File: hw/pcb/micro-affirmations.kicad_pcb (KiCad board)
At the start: 2 copper layers, 100 x 100 mm, 47 parts, among them J1 USB-C_2171750001, Q1 SSM3K37FSLF, Q10 SSM3K37FSLF, Q2 SSM3K37FSLF, Q3 SSM3K37FSLF, Q4 SSM3K37FSLF, Q5 SSM3K37FSLF, Q6 SSM3K37FSLF, Q7 SSM3K37FSLF, Q8 SSM3K37FSLF, Q9 SSM3K37FSLF, SW1 SW_Push, U1 STM32C031C6Tx

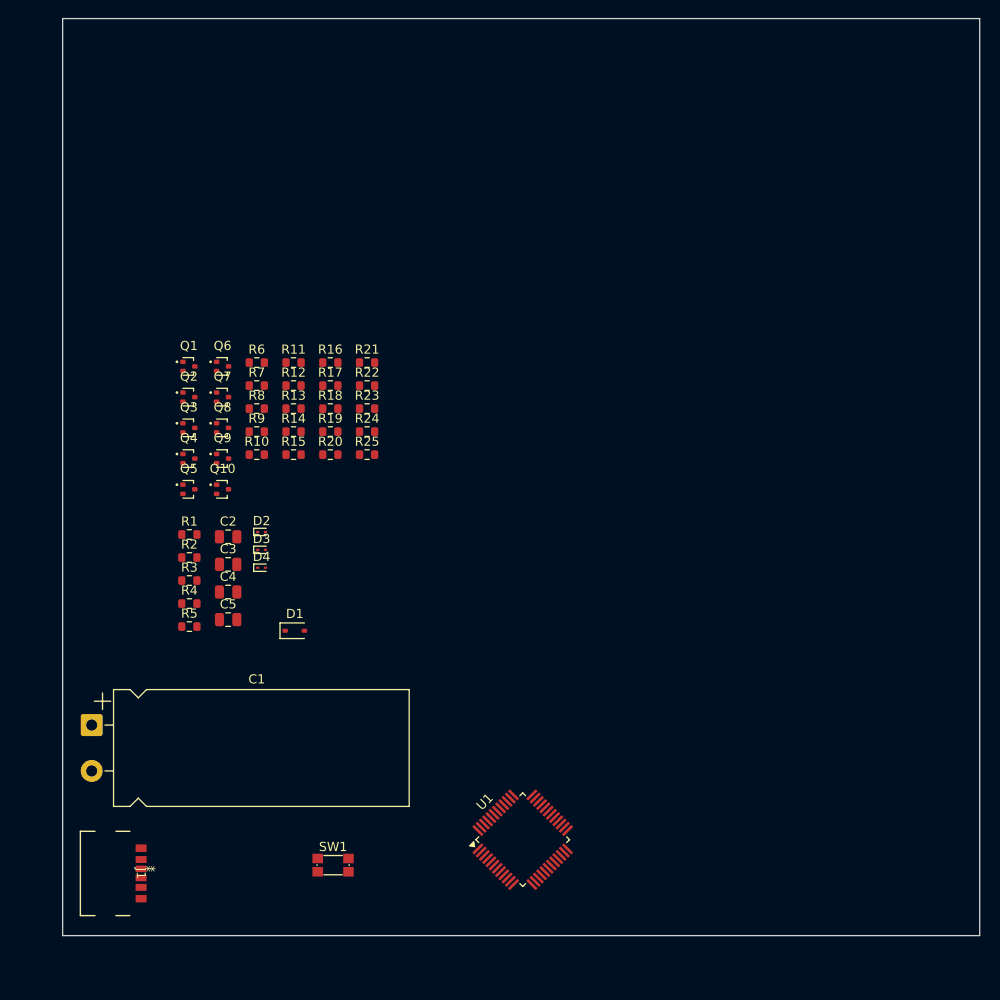
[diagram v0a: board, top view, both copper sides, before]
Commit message: fix: added programming and debug port to schematic
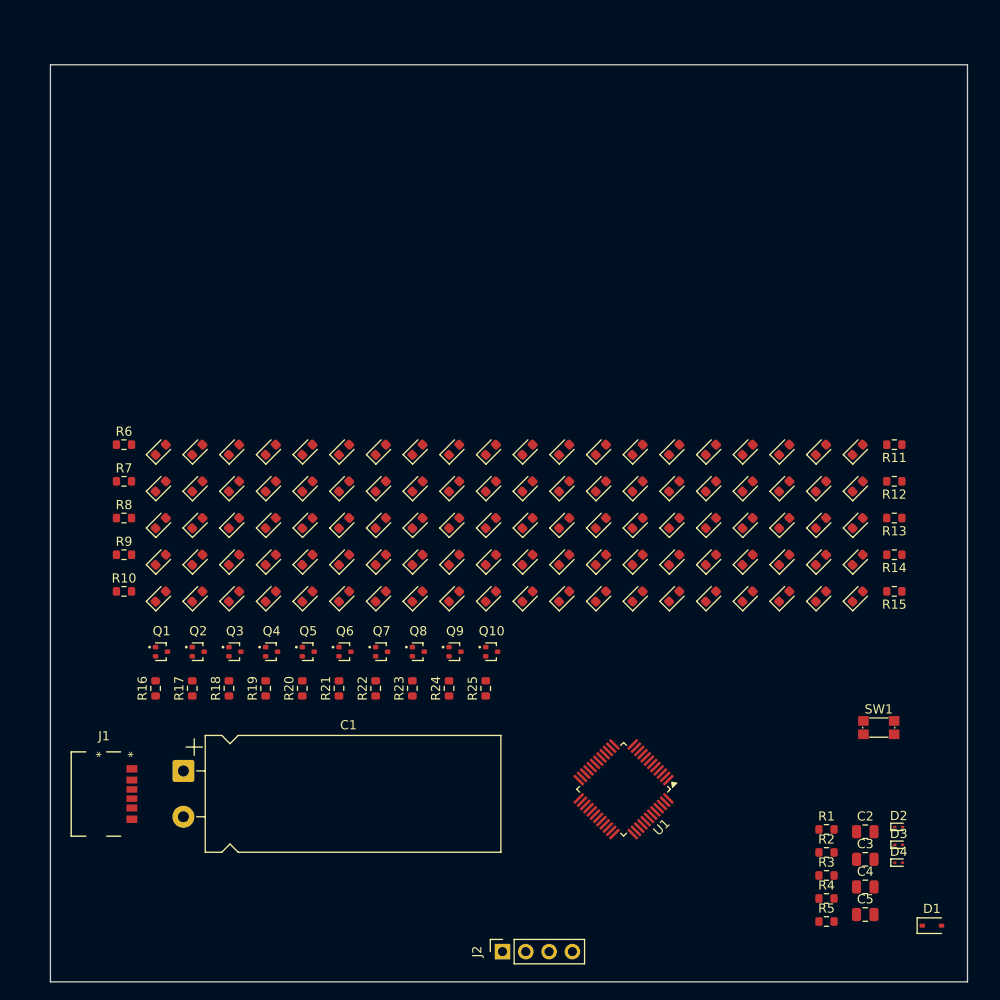
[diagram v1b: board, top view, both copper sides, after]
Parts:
- added D10: LED, Diode_SMD:D_0603_1608Metric, F.Cu at (130.5, 97.0)
- added D100: LED, Diode_SMD:D_0603_1608Metric, F.Cu at (170.5, 113.0)
- added D101: LED, Diode_SMD:D_0603_1608Metric, F.Cu at (174.5, 113.0)
- added D102: LED, Diode_SMD:D_0603_1608Metric, F.Cu at (178.5, 113.0)
- added D103: LED, Diode_SMD:D_0603_1608Metric, F.Cu at (182.5, 113.0)
- added D104: LED, Diode_SMD:D_0603_1608Metric, F.Cu at (186.5, 113.0)
- added D11: LED, Diode_SMD:D_0603_1608Metric, F.Cu at (134.5, 97.0)
- added D12: LED, Diode_SMD:D_0603_1608Metric, F.Cu at (138.5, 97.0)
- added D13: LED, Diode_SMD:D_0603_1608Metric, F.Cu at (142.5, 97.0)
- added D14: LED, Diode_SMD:D_0603_1608Metric, F.Cu at (146.5, 97.0)
- added D15: LED, Diode_SMD:D_0603_1608Metric, F.Cu at (110.5, 101.0)
- added D16: LED, Diode_SMD:D_0603_1608Metric, F.Cu at (114.5, 101.0)
- added D17: LED, Diode_SMD:D_0603_1608Metric, F.Cu at (118.5, 101.0)
- added D18: LED, Diode_SMD:D_0603_1608Metric, F.Cu at (122.5, 101.0)
- added D19: LED, Diode_SMD:D_0603_1608Metric, F.Cu at (126.5, 101.0)
- added D20: LED, Diode_SMD:D_0603_1608Metric, F.Cu at (130.5, 101.0)
- added D21: LED, Diode_SMD:D_0603_1608Metric, F.Cu at (134.5, 101.0)
- added D22: LED, Diode_SMD:D_0603_1608Metric, F.Cu at (138.5, 101.0)
- added D23: LED, Diode_SMD:D_0603_1608Metric, F.Cu at (142.5, 101.0)
- added D24: LED, Diode_SMD:D_0603_1608Metric, F.Cu at (146.5, 101.0)
- added D25: LED, Diode_SMD:D_0603_1608Metric, F.Cu at (110.5, 105.0)
- added D26: LED, Diode_SMD:D_0603_1608Metric, F.Cu at (114.5, 105.0)
- added D27: LED, Diode_SMD:D_0603_1608Metric, F.Cu at (118.5, 105.0)
- added D28: LED, Diode_SMD:D_0603_1608Metric, F.Cu at (122.5, 105.0)
- added D29: LED, Diode_SMD:D_0603_1608Metric, F.Cu at (126.5, 105.0)
- added D30: LED, Diode_SMD:D_0603_1608Metric, F.Cu at (130.5, 105.0)
- added D31: LED, Diode_SMD:D_0603_1608Metric, F.Cu at (134.5, 105.0)
- added D32: LED, Diode_SMD:D_0603_1608Metric, F.Cu at (138.5, 105.0)
- added D33: LED, Diode_SMD:D_0603_1608Metric, F.Cu at (142.5, 105.0)
- added D34: LED, Diode_SMD:D_0603_1608Metric, F.Cu at (146.5, 105.0)
- added D35: LED, Diode_SMD:D_0603_1608Metric, F.Cu at (110.5, 109.0)
- added D36: LED, Diode_SMD:D_0603_1608Metric, F.Cu at (114.5, 109.0)
- added D37: LED, Diode_SMD:D_0603_1608Metric, F.Cu at (118.5, 109.0)
- added D38: LED, Diode_SMD:D_0603_1608Metric, F.Cu at (122.5, 109.0)
- added D39: LED, Diode_SMD:D_0603_1608Metric, F.Cu at (126.5, 109.0)
- added D40: LED, Diode_SMD:D_0603_1608Metric, F.Cu at (130.5, 109.0)
- added D41: LED, Diode_SMD:D_0603_1608Metric, F.Cu at (134.5, 109.0)
- added D42: LED, Diode_SMD:D_0603_1608Metric, F.Cu at (138.5, 109.0)
- added D43: LED, Diode_SMD:D_0603_1608Metric, F.Cu at (142.5, 109.0)
- added D44: LED, Diode_SMD:D_0603_1608Metric, F.Cu at (146.5, 109.0)
- added D45: LED, Diode_SMD:D_0603_1608Metric, F.Cu at (110.5, 113.0)
- added D46: LED, Diode_SMD:D_0603_1608Metric, F.Cu at (114.5, 113.0)
- added D47: LED, Diode_SMD:D_0603_1608Metric, F.Cu at (118.5, 113.0)
- added D48: LED, Diode_SMD:D_0603_1608Metric, F.Cu at (122.5, 113.0)
- added D49: LED, Diode_SMD:D_0603_1608Metric, F.Cu at (126.5, 113.0)
- added D5: LED, Diode_SMD:D_0603_1608Metric, F.Cu at (110.5, 97.0)
- added D50: LED, Diode_SMD:D_0603_1608Metric, F.Cu at (130.5, 113.0)
- added D51: LED, Diode_SMD:D_0603_1608Metric, F.Cu at (134.5, 113.0)
- added D52: LED, Diode_SMD:D_0603_1608Metric, F.Cu at (138.5, 113.0)
- added D53: LED, Diode_SMD:D_0603_1608Metric, F.Cu at (142.5, 113.0)
- added D54: LED, Diode_SMD:D_0603_1608Metric, F.Cu at (146.5, 113.0)
- added D55: LED, Diode_SMD:D_0603_1608Metric, F.Cu at (150.5, 97.0)
- added D56: LED, Diode_SMD:D_0603_1608Metric, F.Cu at (154.5, 97.0)
- added D57: LED, Diode_SMD:D_0603_1608Metric, F.Cu at (158.5, 97.0)
- added D58: LED, Diode_SMD:D_0603_1608Metric, F.Cu at (162.5, 97.0)
- added D59: LED, Diode_SMD:D_0603_1608Metric, F.Cu at (166.5, 97.0)
- added D6: LED, Diode_SMD:D_0603_1608Metric, F.Cu at (114.5, 97.0)
- added D60: LED, Diode_SMD:D_0603_1608Metric, F.Cu at (170.5, 97.0)
- added D61: LED, Diode_SMD:D_0603_1608Metric, F.Cu at (174.5, 97.0)
- added D62: LED, Diode_SMD:D_0603_1608Metric, F.Cu at (178.5, 97.0)
- added D63: LED, Diode_SMD:D_0603_1608Metric, F.Cu at (182.5, 97.0)
- added D64: LED, Diode_SMD:D_0603_1608Metric, F.Cu at (186.5, 97.0)
- added D65: LED, Diode_SMD:D_0603_1608Metric, F.Cu at (150.5, 101.0)
- added D66: LED, Diode_SMD:D_0603_1608Metric, F.Cu at (154.5, 101.0)
- added D67: LED, Diode_SMD:D_0603_1608Metric, F.Cu at (158.5, 101.0)
- added D68: LED, Diode_SMD:D_0603_1608Metric, F.Cu at (162.5, 101.0)
- added D69: LED, Diode_SMD:D_0603_1608Metric, F.Cu at (166.5, 101.0)
- added D7: LED, Diode_SMD:D_0603_1608Metric, F.Cu at (118.5, 97.0)
- added D70: LED, Diode_SMD:D_0603_1608Metric, F.Cu at (170.5, 101.0)
- added D71: LED, Diode_SMD:D_0603_1608Metric, F.Cu at (174.5, 101.0)
- added D72: LED, Diode_SMD:D_0603_1608Metric, F.Cu at (178.5, 101.0)
- added D73: LED, Diode_SMD:D_0603_1608Metric, F.Cu at (182.5, 101.0)
- added D74: LED, Diode_SMD:D_0603_1608Metric, F.Cu at (186.5, 101.0)
- added D75: LED, Diode_SMD:D_0603_1608Metric, F.Cu at (150.5, 105.0)
- added D76: LED, Diode_SMD:D_0603_1608Metric, F.Cu at (154.5, 105.0)
- added D77: LED, Diode_SMD:D_0603_1608Metric, F.Cu at (158.5, 105.0)
- added D78: LED, Diode_SMD:D_0603_1608Metric, F.Cu at (162.5, 105.0)
- added D79: LED, Diode_SMD:D_0603_1608Metric, F.Cu at (166.5, 105.0)
- added D8: LED, Diode_SMD:D_0603_1608Metric, F.Cu at (122.5, 97.0)
- added D80: LED, Diode_SMD:D_0603_1608Metric, F.Cu at (170.5, 105.0)
- added D81: LED, Diode_SMD:D_0603_1608Metric, F.Cu at (174.5, 105.0)
- added D82: LED, Diode_SMD:D_0603_1608Metric, F.Cu at (178.5, 105.0)
- added D83: LED, Diode_SMD:D_0603_1608Metric, F.Cu at (182.5, 105.0)
- added D84: LED, Diode_SMD:D_0603_1608Metric, F.Cu at (186.5, 105.0)
- added D85: LED, Diode_SMD:D_0603_1608Metric, F.Cu at (150.5, 109.0)
- added D86: LED, Diode_SMD:D_0603_1608Metric, F.Cu at (154.5, 109.0)
- added D87: LED, Diode_SMD:D_0603_1608Metric, F.Cu at (158.5, 109.0)
- added D88: LED, Diode_SMD:D_0603_1608Metric, F.Cu at (162.5, 109.0)
- added D89: LED, Diode_SMD:D_0603_1608Metric, F.Cu at (166.5, 109.0)
- added D9: LED, Diode_SMD:D_0603_1608Metric, F.Cu at (126.5, 97.0)
- added D90: LED, Diode_SMD:D_0603_1608Metric, F.Cu at (170.5, 109.0)
- added D91: LED, Diode_SMD:D_0603_1608Metric, F.Cu at (174.5, 109.0)
- added D92: LED, Diode_SMD:D_0603_1608Metric, F.Cu at (178.5, 109.0)
- added D93: LED, Diode_SMD:D_0603_1608Metric, F.Cu at (182.5, 109.0)
- added D94: LED, Diode_SMD:D_0603_1608Metric, F.Cu at (186.5, 109.0)
- added D95: LED, Diode_SMD:D_0603_1608Metric, F.Cu at (150.5, 113.0)
- added D96: LED, Diode_SMD:D_0603_1608Metric, F.Cu at (154.5, 113.0)
- added D97: LED, Diode_SMD:D_0603_1608Metric, F.Cu at (158.5, 113.0)
- added D98: LED, Diode_SMD:D_0603_1608Metric, F.Cu at (162.5, 113.0)
- added D99: LED, Diode_SMD:D_0603_1608Metric, F.Cu at (166.5, 113.0)
- added J2: DEBUG, Connector_PinSocket_2.54mm:PinSocket_1x04_P2.54mm_Vertical, F.Cu at (147.8, 151.7)
- moved D1 76.6 mm to (194.6, 148.9)
- moved C2 76.6 mm to (187.4, 138.6)
- moved C3 76.6 mm to (187.4, 141.6)
- moved C4 76.6 mm to (187.4, 144.7)
- moved C5 76.6 mm to (187.4, 147.7)
- moved D2 76.6 mm to (191.0, 138.1)
- moved D3 76.6 mm to (191.0, 140.1)
- moved D4 76.6 mm to (191.0, 142.0)
- moved R1 76.6 mm to (183.1, 138.4)
- moved R2 76.6 mm to (183.1, 140.9)
- moved R3 76.6 mm to (183.1, 143.4)
- moved R4 76.6 mm to (183.1, 145.9)
- moved R5 76.6 mm to (183.1, 148.4)
- moved R15 67.2 mm to (190.5, 112.4), turned to 180 degrees
- moved R14 66.9 mm to (190.5, 108.4), turned to 180 degrees
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
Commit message: chore: component footprint layout complete
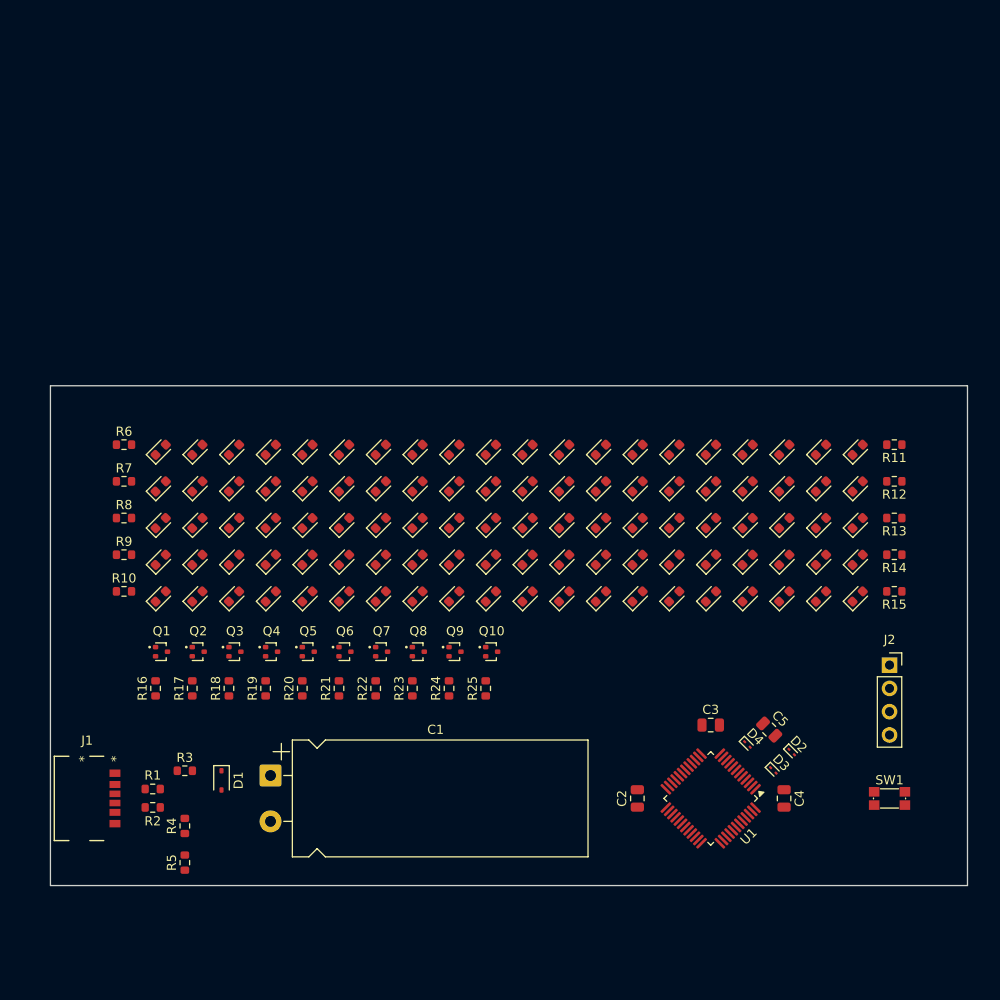
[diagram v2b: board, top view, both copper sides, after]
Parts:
- moved D1 79.1 mm to (117.2, 133.0), turned to -90 degrees
- moved R2 73.6 mm to (109.7, 136.0)
- moved R1 73.6 mm to (109.7, 134.0)
- moved R3 70.9 mm to (113.2, 132.0)
- moved R4 70.4 mm to (113.2, 138.0), turned to 90 degrees
- moved R5 70.3 mm to (113.2, 142.0), turned to 90 degrees
- moved J2 52.5 mm to (190.0, 120.5), turned to 0 degrees
- moved C2 25.1 mm to (162.5, 135.0), turned to 90 degrees
- moved C5 22.7 mm to (176.9, 127.5), turned to -45 degrees
- moved C3 22.3 mm to (170.5, 127.0)
- moved D4 20.9 mm to (174.5, 129.1), turned to -45 degrees
- moved D3 15.9 mm to (177.3, 131.9), turned to -45 degrees
- moved D2 14.2 mm to (179.3, 129.9), turned to -45 degrees
- moved C4 13.1 mm to (178.5, 135.0), turned to -90 degrees
- moved U1 9.55 mm to (170.5, 135.0)
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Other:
- board size 100 x 100 mm -> 100 x 54.5 mm

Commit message: feat: completed pcb layout for revision a
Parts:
- J2: footprint Connector_PinSocket_2.54mm:PinSocket_1x04_P2.54mm_Vertical -> Connector_PinHeader_2.54mm:PinHeader_1x05_P2.54mm_Vertical
- moved J2 1.00 mm to (190.0, 119.5)
- moved Q10 0.96 mm to (145.7, 119.0)
- moved Q6 0.96 mm to (129.7, 119.0)
- moved Q7 0.96 mm to (133.7, 119.0)
- moved Q8 0.96 mm to (137.7, 119.0)
- moved Q9 0.96 mm to (141.7, 119.0)
- moved R16 0.96 mm to (109.0, 123.0)
- moved R17 0.96 mm to (113.0, 123.0)
- moved R18 0.96 mm to (117.0, 123.0)
- moved R19 0.96 mm to (121.0, 123.0)
- moved R20 0.96 mm to (125.0, 123.0)
- moved R21 0.96 mm to (129.0, 123.0)
- moved R22 0.96 mm to (133.0, 123.0)
- moved R23 0.96 mm to (137.0, 123.0)
- moved R24 0.96 mm to (141.0, 123.0)
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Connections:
- J2 pad 2: /DEBUG_SWCLK -> /NRST
- J2 pad 3: /DEBUG_SWDIO -> /DEBUG_SWCLK
- J2 pad 4: +3V0 -> /DEBUG_SWDIO
- U1 pad 25: /MATRIX_A9 -> /MATRIX_A4
- U1 pad 26: /MATRIX_A8 -> /MATRIX_A3
- U1 pad 27: /MATRIX_A7 -> /MATRIX_A2
- U1 pad 28: /MATRIX_A6 -> /MATRIX_A1
- U1 pad 29: /MATRIX_A5 -> /MATRIX_A0
- U1 pad 30: /MATRIX_A4 -> /MATRIX_A5
- U1 pad 31: /MATRIX_A3 -> /MATRIX_A6
- U1 pad 32: /MATRIX_A2 -> /MATRIX_A7
- U1 pad 37: /MATRIX_A1 -> /MATRIX_A8
- U1 pad 38: /MATRIX_A0 -> /MATRIX_A9
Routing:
- net Net-(D15-K): track 0.00 -> 104.6 mm, vias 0 -> 12
- net /MATRIX_A0: track 0.00 -> 104.6 mm, vias 0 -> 2
- net Net-(D16-K): track 0.00 -> 102.6 mm, vias 0 -> 12
- net Net-(D17-K): track 0.00 -> 100.6 mm, vias 0 -> 12
- net Net-(D18-K): track 0.00 -> 98.6 mm, vias 0 -> 12
- net /MATRIX_A1: track 0.00 -> 98.0 mm, vias 0 -> 2
- net Net-(D10-K): track 0.00 -> 96.7 mm, vias 0 -> 11
- net Net-(D19-K): track 0.00 -> 96.6 mm, vias 0 -> 12
- net Net-(D101-K): track 0.00 -> 95.3 mm, vias 0 -> 11
- net +3V0: track 0.00 -> 94.8 mm, vias 0 -> 5
- net Net-(D102-K): track 0.00 -> 93.9 mm, vias 0 -> 11
- net Net-(D103-K): track 0.00 -> 92.5 mm, vias 0 -> 11
- net /MATRIX_A2: track 0.00 -> 91.3 mm, vias 0 -> 2
- net Net-(D104-K): track 0.00 -> 90.5 mm, vias 0 -> 10
- net /MATRIX_A3: track 0.00 -> 84.7 mm, vias 0 -> 2
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- added copper zone on B.Cu, net GND
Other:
- board text added: "${COMPANY}"
- board text added: "${REVISION}"
- board text added: "${TITLE}"
- board text added: "+3V0"
- board text added: "Donut Remover"
- board text added: "GND"
- board text added: "NRST"
- board text added: "SWCLK"
- board text added: "SWDIO"
